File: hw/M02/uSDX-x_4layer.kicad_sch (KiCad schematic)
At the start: 89 parts, among them J1 DC Jack, J10 1602LCD, J11 PJ-324M, J12 PJ-324M, J13 PA MOSFETs, J2 FilterConn, J3 Antenna, J4 Etherkit si5351, J5 EK CLK0, J6 EK CLK1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

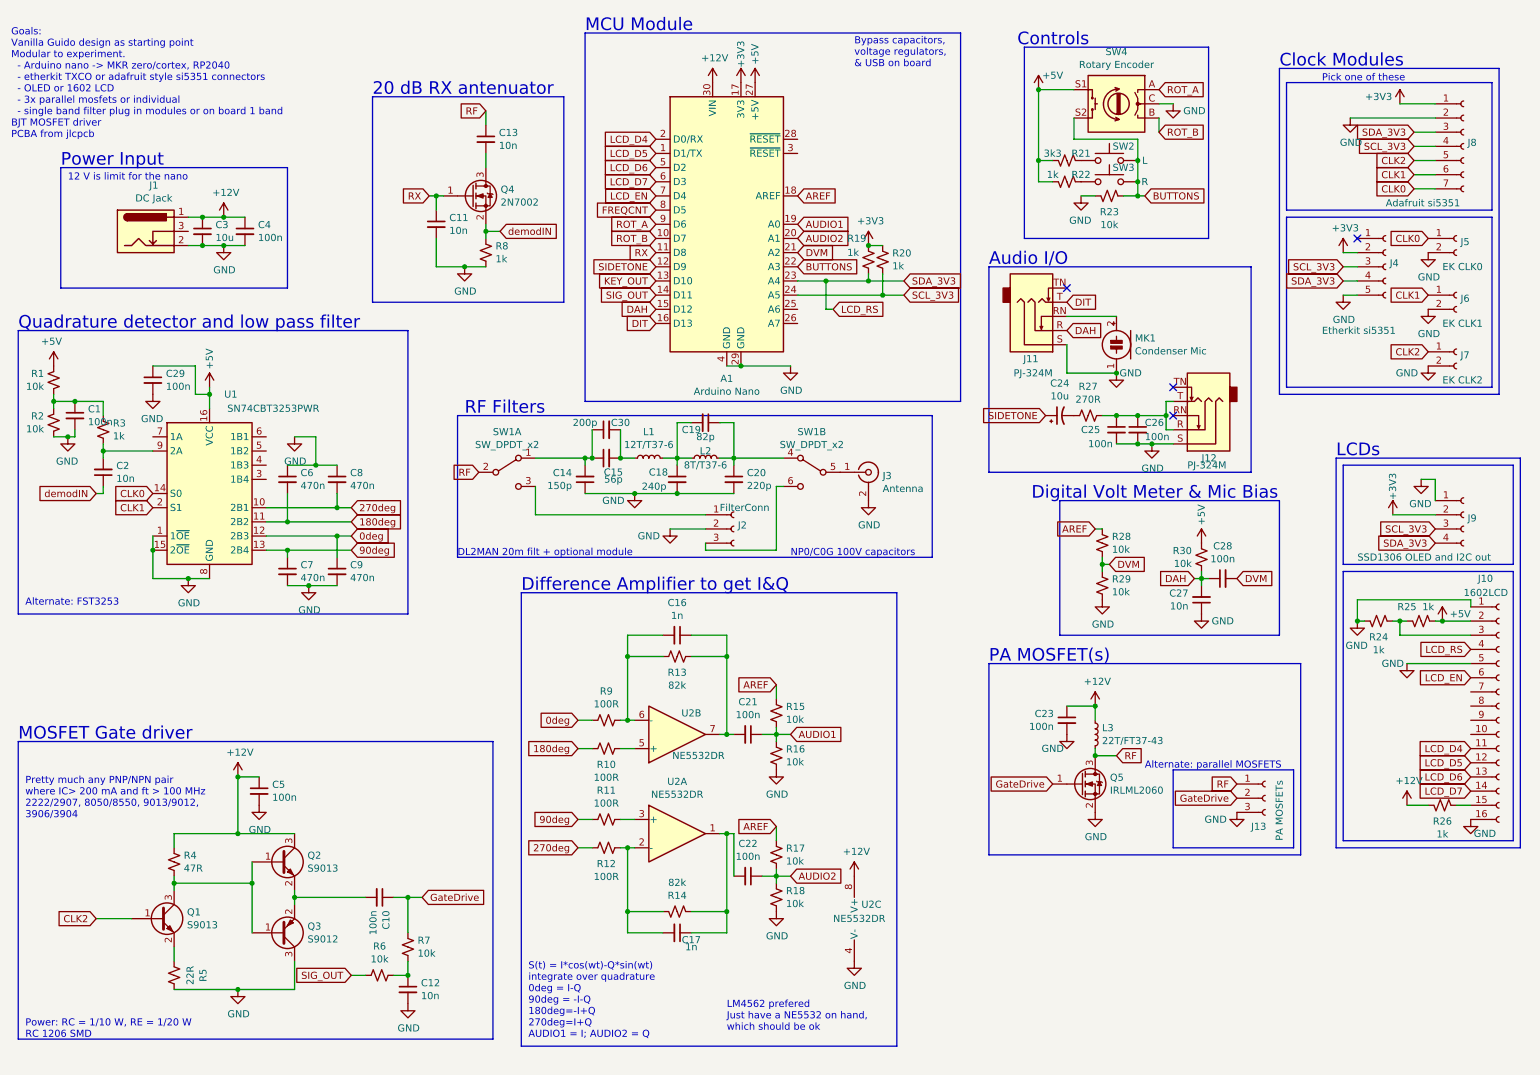
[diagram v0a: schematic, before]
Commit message: Leveraging uSDX-x to become M2 hardware
Replace Arduino MCU with Raspberry Pi
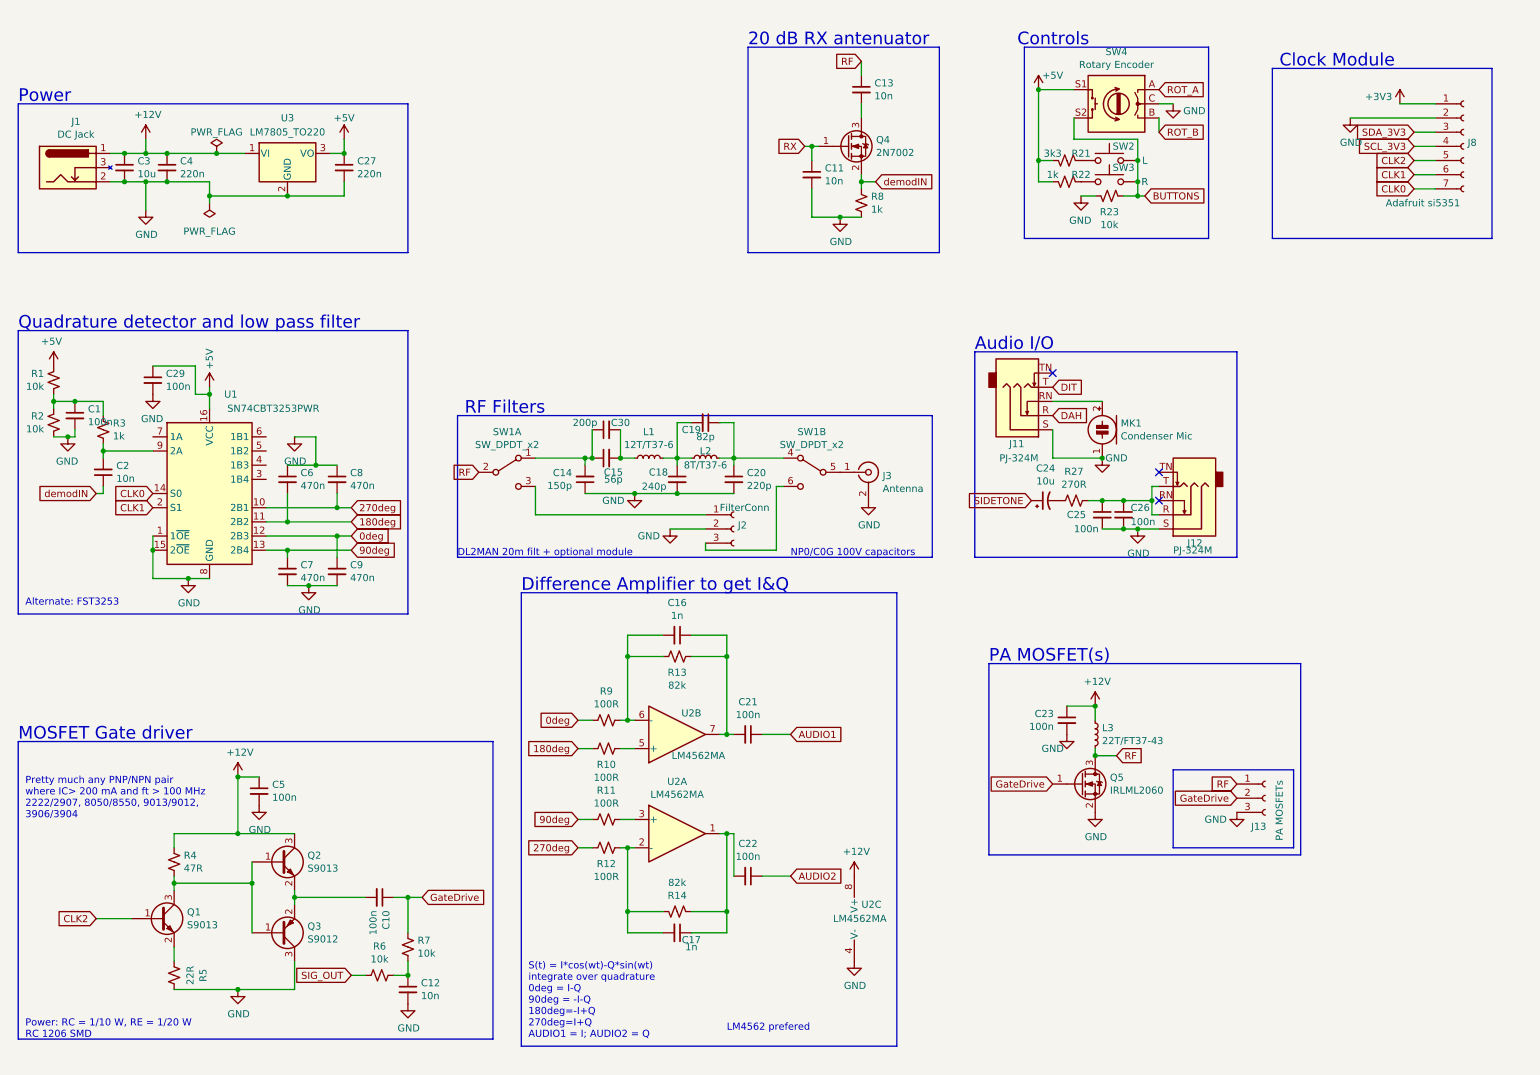
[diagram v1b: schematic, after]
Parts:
- removed A1: Arduino Nano, Module:Arduino_Nano, symbol MCU_Module:Arduino_Nano_v2.x
- removed C28: 100n, Capacitor_SMD:C_0805_2012Metric_Pad1.15x1.40mm_HandSolder, symbol Device:C_Small
- removed J10: 1602LCD, uSDX-x:WC1602A, symbol uSDX-x-rescue:Conn_01x16_Female-Connector
- removed J4: Etherkit si5351, Connector_PinSocket_2.54mm:PinSocket_1x05_P2.54mm_Vertical, symbol uSDX-x-rescue:Conn_01x05_Female-Connector
- removed J5: EK CLK0, Connector_PinSocket_2.54mm:PinSocket_1x02_P2.54mm_Vertical, symbol uSDX-x-rescue:Conn_01x02_Female-Connector
- removed J6: EK CLK1, Connector_PinSocket_2.54mm:PinSocket_1x02_P2.54mm_Vertical, symbol uSDX-x-rescue:Conn_01x02_Female-Connector
- removed J7: EK CLK2, Connector_PinSocket_2.54mm:PinSocket_1x02_P2.54mm_Vertical, symbol uSDX-x-rescue:Conn_01x02_Female-Connector
- removed J9: SSD1306 OLED and I2C out, Connector_PinSocket_2.54mm:PinSocket_1x04_P2.54mm_Vertical, symbol uSDX-x-rescue:Conn_01x04_Female-Connector
- removed R15, R16, R17, R18, R28, R29, R30: 10k, Resistor_SMD:R_0805_2012Metric_Pad1.15x1.40mm_HandSolder, symbol Device:R_Small_US
- removed R19, R20, R24, R25, R26: 1k, Resistor_SMD:R_0805_2012Metric_Pad1.15x1.40mm_HandSolder, symbol Device:R_Small_US
- added U3: LM7805_TO220, Package_TO_SOT_THT:TO-220-3_Vertical, symbol Regulator_Linear:LM7805_TO220
- C27: value 10n -> 220n; LCSC C1710 -> C49678
- C4: value 100n -> 220n
- U2: value NE5532DR -> LM4562MA
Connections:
- net +12V: now also U3.1 (VI)
- net +5V: now also C27.1, U3.3 (VO)
- net DAH: no longer C27.2
- net GND: now also C27.2, U3.2 (GND); no longer C27.1
- net LCD_RS renamed SDA_3V3
- no-connect marks 4 -> 3
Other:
- note added: "Clock Module"
- note added: "LM4562 prefered"
- note added: "Power"
- note removed: "12 V is limit for the nano"
- note removed: "Alternate: parallel MOSFETS"
- note removed: "Bypass capacitors, voltage regulators, & USB on board"
- note removed: "Clock Modules"
- note removed: "Digital Volt Meter & Mic Bias"
- note removed: "Goals: Vanilla Guido design as starting point Modular to experiment. - Arduino nano -> MKR zero/cortex, RP2040 - etherkit TXCO or adafruit style si5351 connectors - OLED or 1602 LCD - 3x parallel mosfets or individual - single band filter plug in modules or on board 1 band BJT MOSFET driver PCBA from jlcpcb"
- note removed: "LCDs"
- note removed: "LM4562 prefered Just have a NE5532 on hand, which should be ok"
- note removed: "MCU Module"
- note removed: "Pick one of these"
- note removed: "Power Input"
- moved on the sheet: C11, C13, C24, C25, C26, C3, C4, J11, J12, MK1, Q4, R27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

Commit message: Early board development and CAT investigation
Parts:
- removed C24: 10u, Capacitor_SMD:C_0805_2012Metric_Pad1.15x1.40mm_HandSolder, symbol uSDX-x-rescue:CP1_Small-Device
- removed C25, C26: 100n, Capacitor_SMD:C_0805_2012Metric_Pad1.15x1.40mm_HandSolder, symbol Device:C_Small
- removed J11, J12: PJ-324M, Connector_Audio:Jack_3.5mm_Ledino_KB3SPRS_Horizontal, symbol uSDX-x-rescue:AudioJack3_SwitchTR-Connector
- removed J13: PA MOSFETs, Connector_PinSocket_2.54mm:PinSocket_1x03_P2.54mm_Vertical, symbol uSDX-x-rescue:Conn_01x03_Female-Connector
- removed MK1: Condenser Mic, Connector_PinSocket_2.54mm:PinSocket_1x02_P2.54mm_Vertical, symbol Device:Microphone_Condenser
- removed R27: 270R, Resistor_SMD:R_0805_2012Metric_Pad1.15x1.40mm_HandSolder, symbol Device:R_Small_US
- added CON1: SJ1-3523N, digikey-footprints:Headphone_Jack_3.5mm_SJ1-3523N, symbol dk_Barrel-Audio-Connectors:SJ1-3523N
- added J4: RASPBERRYPI-40-PIN-GPIO_PTH, 2X20_SHROUDED, symbol SparkFun-Connectors:RASPBERRYPI-40-PIN-GPIO_PTH
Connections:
- net GND: now also CON1.1 (S), J4.14 (GND), J4.20 (GND), J4.25 (GND), J4.30 (GND), J4.34 (GND), J4.39 (GND), J4.6 (GND), J4.9 (GND)
- net AUDIO1: no longer names the net of C21.1
- net AUDIO1: now also CON1.3 (R)
- net AUDIO2: no longer names the net of C22.1
- net AUDIO2: now also CON1.2 (T)
- net SCL_3V3 renamed SCL
- net SCL: now also J4.5 (SCL)
- net SDA_3V3 renamed SDA
- net SDA: now also J4.3 (SDA)
- no-connect marks 3 -> 0
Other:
- note added: "I"
- note added: "Q"
- note added: "Raspberry GPIO"
- note removed: "Audio I/O"
- company: KD9PDP -> KQ7B derivative of KD9PDP uSDX-x
- title: uSDX-X -> yasdr
- moved on the sheet: C1, C10, C11, C12, C13, C14, C15, C16, C17, C18, C19, C2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

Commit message: Fixup kcad crash
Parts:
- J4:  CONN-12263 -> (none); LCSC (none) -> CONN-12263
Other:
- note added: "Pretty much any PNP/NPN pair where IC>200 mA and ft>100 MHz. E.G. 2222/2907, 8050/8550, 9013/9012, 3906/3904."
- note added: "VFO Module"
- note removed: "Clock Module"
- note removed: "Pretty much any PNP/NPN pair where IC> 200 mA and ft > 100 MHz 2222/2907, 8050/8550, 9013/9012, 3906/3904"
- moved on the sheet: C10, C12, C16, C17, C21, C22, C23, C27, C3, C4, C5, CON1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
